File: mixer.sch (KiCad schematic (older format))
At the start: 27 parts

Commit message: Schematic finished
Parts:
- gave numbers to parts that had none: 27
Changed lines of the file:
@@
 LIBS:2450bl15b050
 LIBS:tlv4172
+LIBS:l4940d2t12-tr
+LIBS:tps54308
+LIBS:l78l33abu
+LIBS:adp150aujz-18
 LIBS:radar-cache
+LIBS:hn1c01fu
 EELAYER 25 0
 EELAYER END
 $Descr A4 11693 8268
 encoding utf-8
-Sheet 5 7
+Sheet 5 8
 Title ""
 Date ""
@@
 $EndDescr
 $Comp
-L AD8343 U?
+L AD8343 U501
 U 1 1 59D581AC
 P 6040 3700
-F 0 "U?" H 6040 4250 60  0000 C CNN
+F 0 "U501" H 6040 4250 60  0000 C CNN
 F 1 "AD8343" H 6440 3100 60  0000 C CNN
 F 2 "" H 6040 3700 60  0001 C CNN
@@
 $EndComp
 $Comp
-L 2450BL15B100 T?
+L 2450BL15B100 T502
 U 1 1 59D58FE9
 P 3340 3450
-F 0 "T?" H 3340 3550 60  0000 C CNN
+F 0 "T502" H 3340 3550 60  0000 C CNN
 F 1 "2450BL15B100" H 3790 3300 60  0000 C CNN
 F 2 "" H 3340 3450 60  0001 C CNN
@@
 $EndComp
 $Comp
-L taper T?
+L taper T501
 U 1 1 59D59667
 P 2810 3060
-F 0 "T?" H 2810 3210 60  0000 C CNN
+F 0 "T501" H 2810 3210 60  0000 C CNN
 F 1 "taper" H 2710 2910 60  0000 C CNN
 F 2 "" H 2810 3060 60  0001 C CNN
@@
 $EndComp
 $Comp
-L GND #PWR?
+L GND #PWR042
 U 1 1 59D5980B
 P 3670 3140
-F 0 "#PWR?" H 3670 2890 50  0001 C CNN
+F 0 "#PWR042" H 3670 2890 50  0001 C CNN
 F 1 "GND" H 3670 2990 50  0000 C CNN
 F 2 "" H 3670 3140 50  0001 C CNN
@@
 $EndComp
 $Comp
-L GND #PWR?
+L GND #PWR043
 U 1 1 59D5982F
 P 3390 3770
-F 0 "#PWR?" H 3390 3520 50  0001 C CNN
+F 0 "#PWR043" H 3390 3520 50  0001 C CNN
 F 1 "GND" H 3390 3620 50  0000 C CNN
 F 2 "" H 3390 3770 50  0001 C CNN
@@
 $EndComp
 $Comp
-L L_Small L?
+L L_Small L501
 U 1 1 59D5994B
 P 3720 3540
-F 0 "L?" H 3750 3580 50  0000 L CNN
+F 0 "L501" H 3750 3580 50  0000 L CNN
 F 1 "2.5n" H 3750 3500 50  0000 L CNN
 F 2 "" H 3720 3540 50  0001 C CNN
@@
 $EndComp
 $Comp
-L C_Small C?
+L C_Small C506
 U 1 1 59D599A4
 P 3920 3400
-F 0 "C?" H 3930 3470 50  0000 L CNN
+F 0 "C506" H 3930 3470 50  0000 L CNN
 F 1 "1p35" H 3930 3320 50  0000 L CNN
 F 2 "" H 3920 3400 50  0001 C CNN
@@
 $EndComp
 $Comp
-L C_Small C?
+L C_Small C508
 U 1 1 59D59B38
 P 3910 3680
-F 0 "C?" H 3920 3750 50  0000 L CNN
+F 0 "C508" H 3920 3750 50  0000 L CNN
 F 1 "1p35" H 3920 3600 50  0000 L CNN
 F 2 "" H 3910 3680 50  0001 C CNN
@@
 $EndComp
 $Comp
-L GND #PWR?
+L GND #PWR044
 U 1 1 59D59D07
 P 6040 4480
-F 0 "#PWR?" H 6040 4230 50  0001 C CNN
+F 0 "#PWR044" H 6040 4230 50  0001 C CNN
 F 1 "GND" H 6040 4330 50  0000 C CNN
 F 2 "" H 6040 4480 50  0001 C CNN
@@
 RF_IN
 $Comp
-L R_Small R?
+L R_Small R507
 U 1 1 59D5A3D3
 P 4240 4220
-F 0 "R?" H 4270 4240 50  0000 L CNN
+F 0 "R507" H 4270 4240 50  0000 L CNN
 F 1 "68.1" H 4270 4180 50  0000 L CNN
 F 2 "" H 4240 4220 50  0001 C CNN
@@
 $EndComp
 $Comp
-L R_Small R?
+L R_Small R508
 U 1 1 59D5A4A9
 P 4390 4220
-F 0 "R?" H 4420 4240 50  0000 L CNN
+F 0 "R508" H 4420 4240 50  0000 L CNN
 F 1 "68.1" H 4420 4180 50  0000 L CNN
 F 2 "" H 4390 4220 50  0001 C CNN
@@
 $EndComp
 $Comp
-L GND #PWR?
+L GND #PWR045
 U 1 1 59D5A4DD
 P 4240 4360
-F 0 "#PWR?" H 4240 4110 50  0001 C CNN
+F 0 "#PWR045" H 4240 4110 50  0001 C CNN
 F 1 "GND" H 4240 4210 50  0000 C CNN
 F 2 "" H 4240 4360 50  0001 C CNN
@@
 $EndComp
 $Comp
-L GND #PWR?
+L GND #PWR046
 U 1 1 59D5A52E
 P 4390 4360
-F 0 "#PWR?" H 4390 4110 50  0001 C CNN
+F 0 "#PWR046" H 4390 4110 50  0001 C CNN
 F 1 "GND" H 4390 4210 50  0000 C CNN
 F 2 "" H 4390 4360 50  0001 C CNN
@@
 $EndComp
 $Comp
-L L_Small L?
+L L_Small L502
 U 1 1 59D5A592
 P 4240 3930
-F 0 "L?" H 4270 3970 50  0000 L CNN
+F 0 "L502" H 4270 3970 50  0000 L CNN
 F 1 "51nH" H 4270 3890 50  0000 L CNN
 F 2 "" H 4240 3930 50  0001 C CNN
@@
 $EndComp
 $Comp
-L L_Small L?
+L L_Small L503
 U 1 1 59D5A69D
 P 4390 3930
-F 0 "L?" H 4420 3970 50  0000 L CNN
+F 0 "L503" H 4420 3970 50  0000 L CNN
 F 1 "51nH" H 4420 3890 50  0000 L CNN
 F 2 "" H 4390 3930 50  0001 C CNN
@@
 NoConn ~ 2830 5290
 $Comp
-L C_Small C?
+L C_Small C511
 U 1 1 59D5C96D
 P 4860 4110
-F 0 "C?" H 4870 4180 50  0000 L CNN
+F 0 "C511" H 4870 4180 50  0000 L CNN
 F 1 "0u1" H 4870 4030 50  0000 L CNN
 F 2 "" H 4860 4110 50  0001 C CNN
@@
 $EndComp
 $Comp
-L R_Small R?
+L R_Small R506
 U 1 1 59D5CB57
 P 5250 4110
-F 0 "R?" H 5280 4130 50  0000 L CNN
+F 0 "R506" H 5280 4130 50  0000 L CNN
 F 1 "0" H 5280 4070 50  0000 L CNN
 F 2 "" H 5250 4110 50  0001 C CNN
@@
 $EndComp
 $Comp
-L GND #PWR?
+L GND #PWR047
 U 1 1 59D5CBC6
 P 5250 4310
-F 0 "#PWR?" H 5250 4060 50  0001 C CNN
+F 0 "#PWR047" H 5250 4060 50  0001 C CNN
 F 1 "GND" H 5250 4160 50  0000 C CNN
 F 2 "" H 5250 4310 50  0001 C CNN
@@
 $EndComp
 $Comp
-L GND #PWR?
+L GND #PWR048
 U 1 1 59D5CBFC
 P 4860 4320
-F 0 "#PWR?" H 4860 4070 50  0001 C CNN
+F 0 "#PWR048" H 4860 4070 50  0001 C CNN
 F 1 "GND" H 4860 4170 50  0000 C CNN
 F 2 "" H 4860 4320 50  0001 C CNN
@@
 $EndComp
 $Comp
-L +5V #PWR?
+L +5V #PWR049
 U 1 1 59D5CE3D
 P 4600 2580
-F 0 "#PWR?" H 4600 2430 50  0001 C CNN
+F 0 "#PWR049" H 4600 2430 50  0001 C CNN
 F 1 "+5V" H 4600 2720 50  0000 C CNN
 F 2 "" H 4600 2580 50  0001 C CNN
@@
 P 7920 3750
 AR Path="/59D5DFCB" Ref="T?"  Part="1"
-AR Path="/59D57E33/59D5DFCB" Ref="T?"  Part="1"
-F 0 "T?" H 7920 3850 60  0000 C CNN
+AR Path="/59D57E33/59D5DFCB" Ref="T504"  Part="1"
+F 0 "T504" H 7920 3850 60  0000 C CNN
 F 1 "2450BL15B050" H 8150 3640 60  0000 C CNN
 F 2 "" H 7920 3750 60  0001 C CNN
@@
 $EndComp
 $Comp
-L GND #PWR?
+L GND #PWR050
 U 1 1 59D5ED7D
 P 8230 3970
-F 0 "#PWR?" H 8230 3720 50  0001 C CNN
+F 0 "#PWR050" H 8230 3720 50  0001 C CNN
 F 1 "GND" H 8230 3820 50  0000 C CNN
 F 2 "" H 8230 3970 50  0001 C CNN
@@
 $EndComp
 $Comp
-L C_Small C?
+L C_Small C510
 U 1 1 59D5EF92
 P 7040 3800
-F 0 "C?" H 7050 3870 50  0000 L CNN
+F 0 "C510" H 7050 3870 50  0000 L CNN
 F 1 "10n" H 7050 3720 50  0000 L CNN
 F 2 "" H 7040 3800 50  0001 C CNN
@@
 $EndComp
 $Comp
-L C_Small C?
+L C_Small C509
 U 1 1 59D5EFF5
 P 7140 3700
-F 0 "C?" H 7150 3770 50  0000 L CNN
+F 0 "C509" H 7150 3770 50  0000 L CNN
 F 1 "10n" H 7150 3620 50  0000 L CNN
 F 2 "" H 7140 3700 50  0001 C CNN
@@
 $EndComp
 $Comp
-L taper T?
+L taper T503
 U 1 1 59D5F9D7
 P 8540 3700
-F 0 "T?" H 8540 3850 60  0000 C CNN
+F 0 "T503" H 8540 3850 60  0000 C CNN
 F 1 "taper" H 8440 3550 60  0000 C CNN
 F 2 "" H 8540 3700 60  0001 C CNN
@@
 LO_IN
 $Comp
-L C_Small C?
+L C_Small C503
 U 1 1 59D6044F
 P 4600 2860
-F 0 "C?" H 4610 2930 50  0000 L CNN
+F 0 "C503" H 4610 2930 50  0000 L CNN
 F 1 "0u1" H 4610 2780 50  0000 L CNN
 F 2 "" H 4600 2860 50  0001 C CNN
@@
 $EndComp
 $Comp
-L C_Small C?
+L C_Small C504
 U 1 1 59D60529
 P 4950 2860
-F 0 "C?" H 4960 2930 50  0000 L CNN
+F 0 "C504" H 4960 2930 50  0000 L CNN
 F 1 "10n" H 4960 2780 50  0000 L CNN
 F 2 "" H 4950 2860 50  0001 C CNN
@@
 $EndComp
 $Comp
-L R_Small R?
+L R_Small R502
 U 1 1 59D605A3
 P 4810 2670
-F 0 "R?" H 4840 2690 50  0000 L CNN
+F 0 "R502" H 4840 2690 50  0000 L CNN
 F 1 "3.9" H 4840 2630 50  0000 L CNN
 F 2 "" H 4810 2670 50  0001 C CNN
@@
 $EndComp
 $Comp
-L GND #PWR?
+L GND #PWR051
 U 1 1 59D60664
 P 4600 3090
-F 0 "#PWR?" H 4600 2840 50  0001 C CNN
+F 0 "#PWR051" H 4600 2840 50  0001 C CNN
 F 1 "GND" H 4600 2940 50  0000 C CNN
 F 2 "" H 4600 3090 50  0001 C CNN
@@
 $EndComp
 $Comp
-L GND #PWR?
+L GND #PWR052
 U 1 1 59D606AF
 P 4950 3090
-F 0 "#PWR?" H 4950 2840 50  0001 C CNN
+F 0 "#PWR052" H 4950 2840 50  0001 C CNN
 F 1 "GND" H 4950 2940 50  0000 C CNN
 F 2 "" H 4950 3090 50  0001 C CNN
@@
 	5110 3300 5390 3300
 $Comp
-L +5V #PWR?
+L +5V #PWR053
 U 1 1 59D61273
 P 6220 2040
-F 0 "#PWR?" H 6220 1890 50  0001 C CNN
+F 0 "#PWR053" H 6220 1890 50  0001 C CNN
 F 1 "+5V" H 6220 2180 50  0000 C CNN
 F 2 "" H 6220 2040 50  0001 C CNN
@@
 $EndComp
 $Comp
-L C_Small C?
+L C_Small C501
 U 1 1 59D61279
 P 6220 2320
-F 0 "C?" H 6230 2390 50  0000 L CNN
+F 0 "C501" H 6230 2390 50  0000 L CNN
 F 1 "0u1" H 6230 2240 50  0000 L CNN
 F 2 "" H 6220 2320 50  0001 C CNN
@@
 $EndComp
 $Comp
-L C_Small C?
+L C_Small C502
 U 1 1 59D6127F
 P 6570 2320
-F 0 "C?" H 6580 2390 50  0000 L CNN
+F 0 "C502" H 6580 2390 50  0000 L CNN
 F 1 "10n" H 6580 2240 50  0000 L CNN
 F 2 "" H 6570 2320 50  0001 C CNN
@@
 $EndComp
 $Comp
-L R_Small R?
+L R_Small R501
 U 1 1 59D61285
 P 6430 2130
-F 0 "R?" H 6460 2150 50  0000 L CNN
+F 0 "R501" H 6460 2150 50  0000 L CNN
 F 1 "3.9" H 6460 2090 50  0000 L CNN
 F 2 "" H 6430 2130 50  0001 C CNN
@@
 $EndComp
 $Comp
-L GND #PWR?
+L GND #PWR054
 U 1 1 59D6128B
 P 6220 2550
-F 0 "#PWR?" H 6220 2300 50  0001 C CNN
+F 0 "#PWR054" H 6220 2300 50  0001 C CNN
 F 1 "GND" H 6220 2400 50  0000 C CNN
 F 2 "" H 6220 2550 50  0001 C CNN
@@
 $EndComp
 $Comp
-L GND #PWR?
+L GND #PWR055
 U 1 1 59D61291
 P 6570 2550
-F 0 "#PWR?" H 6570 2300 50  0001 C CNN
+F 0 "#PWR055" H 6570 2300 50  0001 C CNN
 F 1 "GND" H 6570 2400 50  0000 C CNN
 F 2 "" H 6570 2550 50  0001 C CNN
@@
 	6730 2760 7160 2760
 $Comp
-L R_Small R?
+L R_Small R503
 U 1 1 59D612B9
 P 7000 3020
-F 0 "R?" H 7030 3040 50  0000 L CNN
+F 0 "R503" H 7030 3040 50  0000 L CNN
 F 1 "200" H 7030 2980 50  0000 L CNN
 F 2 "" H 7000 3020 50  0001 C CNN
@@
 $EndComp
 $Comp
-L R_Small R?
+L R_Small R504
 U 1 1 59D61363
 P 7160 3020
-F 0 "R?" H 7190 3040 50  0000 L CNN
+F 0 "R504" H 7190 3040 50  0000 L CNN
 F 1 "200" H 7190 2980 50  0000 L CNN
 F 2 "" H 7160 3020 50  0001 C CNN
@@
 $EndComp
 $Comp
-L R_Small R?
+L R_Small R505
 U 1 1 59D6145D
 P 7370 3340
-F 0 "R?" H 7400 3360 50  0000 L CNN
+F 0 "R505" H 7400 3360 50  0000 L CNN
 F 1 "400" H 7400 3300 50  0000 L CNN
 F 2 "" H 7370 3340 50  0001 C CNN
@@
 Connection ~ 7000 3500
 $Comp
-L C_Small C?
+L C_Small C507
 U 1 1 59D619DF
 P 7660 3500
-F 0 "C?" H 7670 3570 50  0000 L CNN
+F 0 "C507" H 7670 3570 50  0000 L CNN
 F 1 "1u" H 7670 3420 50  0000 L CNN
 F 2 "" H 7660 3500 50  0001 C CNN
@@
 $EndComp
 $Comp
-L C_Small C?
+L C_Small C505
 U 1 1 59D61A80
 P 7660 3190
-F 0 "C?" H 7670 3260 50  0000 L CNN
+F 0 "C505" H 7670 3260 50  0000 L CNN
 F 1 "1u" H 7670 3110 50  0000 L CNN
 F 2 "" H 7660 3190 50  0001 C CNN

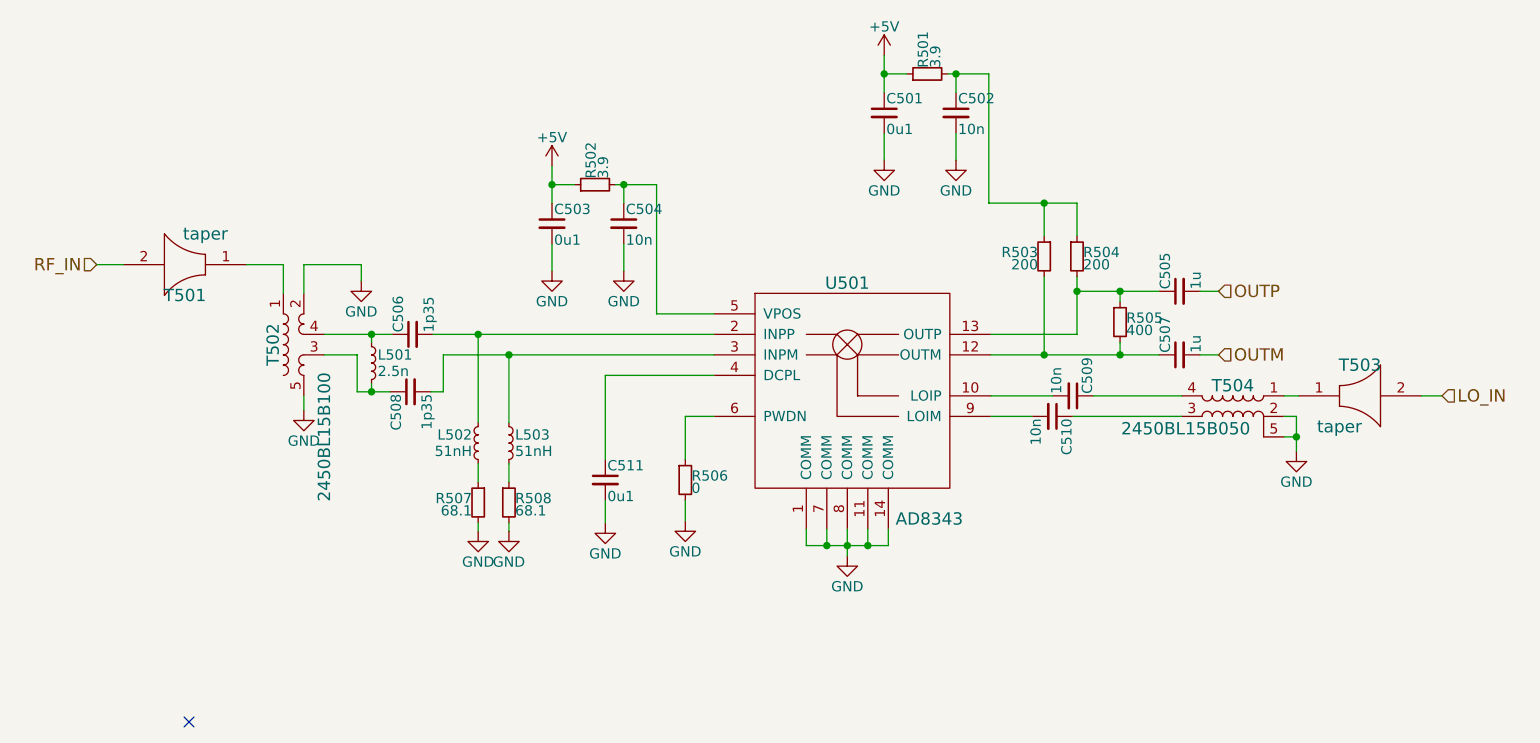
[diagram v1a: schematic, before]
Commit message: Assign a lot of footprints, fix l78l33abu part (input and output were reversed)
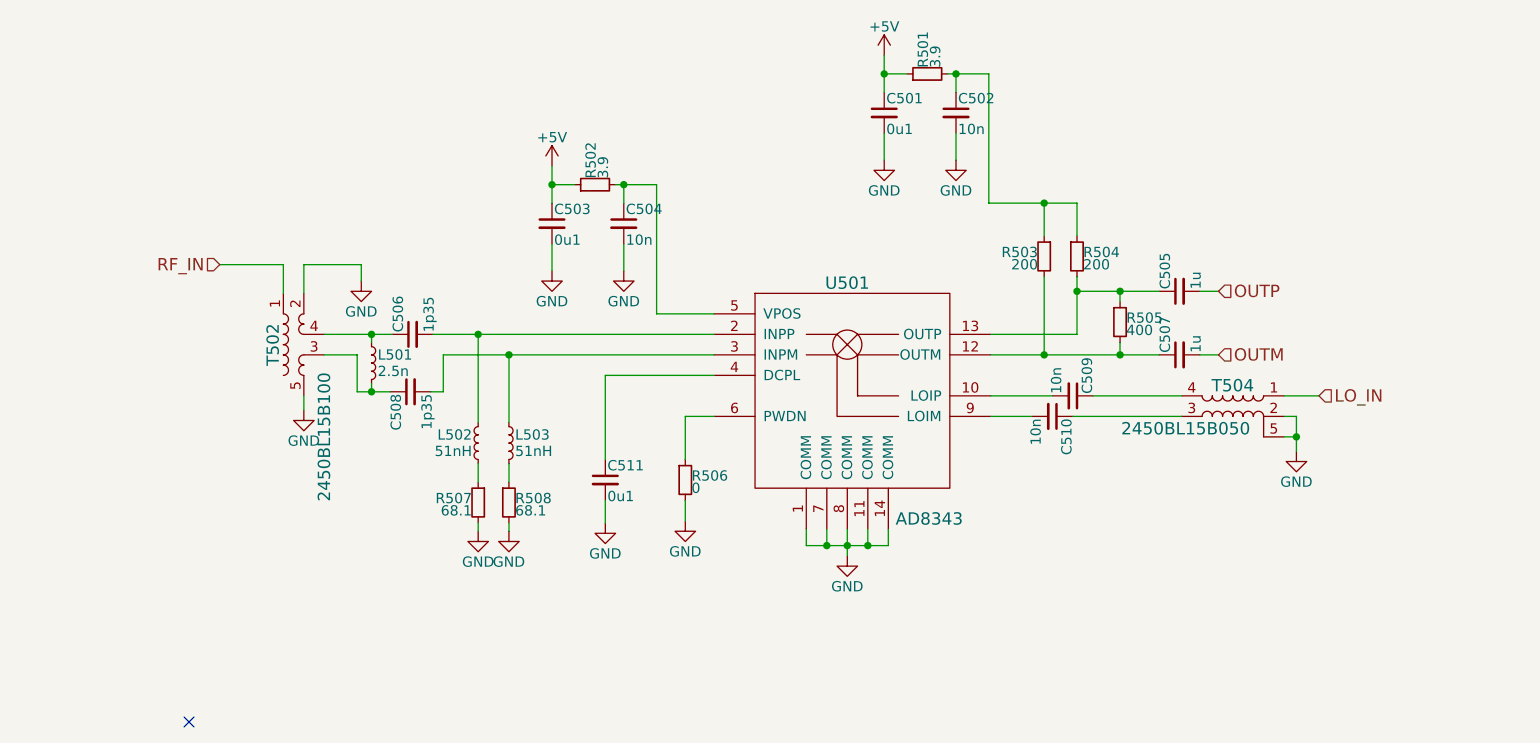
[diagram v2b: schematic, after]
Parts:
- removed T501, T503: taper, symbol taper
- C501, C503, C505, C507, C511: footprint (none) -> Capacitors_SMD:C_0603_HandSoldering
- C502, C504, C509, C510, L502, L503: footprint (none) -> Capacitors_SMD:C_0402
- C506, C508, L501: footprint (none) -> Capacitors_SMD:C_0201
- R501, R502, R506: footprint (none) -> Resistors_SMD:R_0603_HandSoldering
- R503, R504, R505, R507, R508: footprint (none) -> Resistors_SMD:R_1206_HandSoldering
- T502, T504: footprint (none) -> rajsradar:2450BL15B100
- U501: footprint (none) -> Housings_SSOP:TSSOP-14_4.4x5mm_Pitch0.65mm
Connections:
- net LO_IN: now also T504.1
- net RF_IN: now also T502.1
